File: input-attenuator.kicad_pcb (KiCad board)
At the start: 2 copper layers, 100.1 x 56.4 mm, 44 parts, among them J1 DC_INTF, J2 RF_IN, J3 RX_1_RF, J4 RX_2_RF, K1 EE2-5TNU-L, K2 EE2-5TNU-L, K3 EE2-5TNU-L, K4 EE2-5TNU-L, Q1 MMBT3904, Q2 MMBT3904, Q3 MMBT3904, Q4 MMBT3904, Q5 MMBT3904, Q6 MMBT3904, Q7 MMBT3904, Q8 MMBT3904, U1 74HC595

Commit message: relaysPlaced
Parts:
- added C3: 0.22u, Capacitor_SMD:C_0805_2012Metric, F.Cu at (132.0, 56.6)
- added C4: 0.22u, Capacitor_SMD:C_0805_2012Metric, F.Cu at (120.3, 56.6)
- added C5: 0.22u, Capacitor_SMD:C_0805_2012Metric, F.Cu at (98.5, 56.4)
- added C6: 0.22u, Capacitor_SMD:C_0805_2012Metric, F.Cu at (87.3, 56.4)
- added Q9: BC858, Package_TO_SOT_SMD:SOT-23, F.Cu at (87.8, 52.1)
- added R18: _, Resistor_SMD:R_0805_2012Metric, F.Cu at (87.3, 31.8)
- added R19: 14.0_, Resistor_SMD:R_0805_2012Metric, F.Cu at (84.7, 31.8)
- added R20: 14.0_, Resistor_SMD:R_0805_2012Metric, F.Cu at (82.2, 31.8)
- added R21: _, Resistor_SMD:R_0805_2012Metric, F.Cu at (79.7, 31.8)
- added R22: 22K, Resistor_SMD:R_0805_2012Metric, F.Cu at (122.6, 52.1)
- added R23: 22K, Resistor_SMD:R_0805_2012Metric, F.Cu at (128.7, 52.1)
- added R24: 22K, Resistor_SMD:R_0805_2012Metric, F.Cu at (93.6, 52.1)
- added R25: 22K, Resistor_SMD:R_0805_2012Metric, F.Cu at (99.7, 52.1)
- added R26: 22K, Resistor_SMD:R_0805_2012Metric, F.Cu at (78.7, 52.1)
- added R27: 22K, Resistor_SMD:R_0805_2012Metric, F.Cu at (84.7, 52.1)
- added R28: 1M, Resistor_SMD:R_0805_2012Metric, F.Cu at (132.0, 60.7)
- added R29: 1M, Resistor_SMD:R_0805_2012Metric, F.Cu at (98.5, 60.5)
- added R30: 1M, Resistor_SMD:R_0805_2012Metric, F.Cu at (87.3, 60.2)
- added U2: 74HC00, Package_SO:SO-14_3.9x8.65mm_P1.27mm, F.Cu at (92.9, 58.9)
- added U3: 74HC00, Package_SO:SO-14_3.9x8.65mm_P1.27mm, F.Cu at (82.0, 58.9)
- added U4: 74HC00, Package_SO:SO-14_3.9x8.65mm_P1.27mm, F.Cu at (126.4, 59.2)
- added U5: 74HC00, Package_SO:SO-14_3.9x8.65mm_P1.27mm, F.Cu at (105.1, 59.2)
- added U6: 74HC595, Package_SO:SO-16_5.3x10.2mm_P1.27mm, F.Cu at (70.6, 58.4)
- Q1, Q2, Q4, Q5, Q6, Q7, Q8: value MMBT3904 -> BC858
- R10, R6: value 22K -> 82.2
- R11, R15, R16, R5: value 22K -> _
- R12: value 40.9 -> 82.2
- R13: value 40.9 -> _
- R14: value 10.1 -> 14.0_
- R17: value 22K -> 14.0_
- R2: value 14.0 -> 22K
- R3: value 14.0 -> 1M
- R4: value 82.2 -> 14.0_
- R7: value 26.0 -> _
- R8: value 26.0 -> 14.0_
- R9: value 35.1 -> _
- U1: value 74HC595 -> 74HC00; footprint Package_SO:SO-16_5.3x10.2mm_P1.27mm -> Package_SO:SO-14_3.9x8.65mm_P1.27mm
- moved D8 88.0 mm to (77.1, 31.8), turned to 90 degrees
- moved J3 80.8 mm to (70.8, 40.6), turned to 90 degrees
- moved D7 79.4 mm to (76.1, 47.0), turned to 90 degrees
- moved J2 74.8 mm to (139.9, 49.3), turned to 135 degrees
- moved Q8 72.7 mm to (81.7, 52.1), turned to 90 degrees
- moved R17 72.0 mm to (94.7, 31.8), turned to -90 degrees
- moved R16 69.5 mm to (97.2, 31.8), turned to 90 degrees
- moved K4 62.4 mm to (83.2, 41.9), turned to 180 degrees
- moved R12 61.2 mm to (80.9, 28.4)
- moved R13 57.9 mm to (86.0, 28.4)
- moved J1 53.8 mm to (72.1, 75.4)
- moved R5 51.6 mm to (114.5, 31.8)
- moved Q7 49.1 mm to (102.8, 52.1), turned to 90 degrees
- moved Q3 48.1 mm to (120.8, 83.0)
- moved D6 46.7 mm to (92.1, 31.8), turned to 90 degrees
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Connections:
- C1 pad 1: VRelay -> +5V
- C2 pad 2: VRelay -> +5V
- D1 pad 1: VRelay -> Net-(D1-Pad1)
- D1 pad 2: Net-(D1-Pad2) -> GND
- D2 pad 1: VRelay -> Net-(D2-Pad1)
- D2 pad 2: Net-(D2-Pad2) -> GND
- D3 pad 1: VRelay -> Net-(D3-Pad1)
- D3 pad 2: Net-(D3-Pad2) -> GND
- D4 pad 1: VRelay -> Net-(D4-Pad1)
- D4 pad 2: Net-(D4-Pad2) -> GND
- D5 pad 1: VRelay -> Net-(D5-Pad1)
- D5 pad 2: Net-(D5-Pad2) -> GND
- D6 pad 1: VRelay -> Net-(D6-Pad1)
- D6 pad 2: Net-(D6-Pad2) -> GND
- D7 pad 1: VRelay -> Net-(D7-Pad1)
- D7 pad 2: Net-(D7-Pad2) -> GND
- D8 pad 1: VRelay -> Net-(D8-Pad1)
- D8 pad 2: Net-(D8-Pad2) -> GND
- J1 pad 1: VRelay -> +5V
- J2 pad 1: RF_IN -> /RF_TX
- J3 pad 1: RX_1_RF -> /RF_RX
- J4 pad 1: RX_2_RF -> /Antenna
- K1 pad 1: VRelay -> GND
- K1 pad 12: Net-(D1-Pad2) -> Net-(D2-Pad1)
- K1 pad 4: RF_IN -> Net-(K1-Pad4)
- K1 pad 6: VRelay -> GND
- K1 pad 7: Net-(D2-Pad2) -> Net-(D1-Pad1)
- K2 pad 1: VRelay -> GND
- K2 pad 10: Net-(K2-Pad10) -> /RF_TX
- K2 pad 12: Net-(D3-Pad2) -> Net-(D3-Pad1)
- K2 pad 3: Net-(K2-Pad10) -> /RF_TX
- K2 pad 4: Net-(K1-Pad9) -> /Antenna
- K2 pad 5: Net-(K2-Pad5) -> Net-(K1-Pad4)
- K2 pad 6: VRelay -> GND
- K2 pad 7: Net-(D4-Pad2) -> Net-(D4-Pad1)
- K2 pad 8: Net-(K2-Pad8) -> Net-(K1-Pad4)
- K2 pad 9: Net-(K2-Pad9) -> /Antenna
- K3 pad 1: VRelay -> GND
- K3 pad 12: Net-(D5-Pad2) -> Net-(D5-Pad1)
- K3 pad 4: Net-(K2-Pad9) -> Net-(K1-Pad9)
- K3 pad 6: VRelay -> GND
- K3 pad 7: Net-(D6-Pad2) -> Net-(D6-Pad1)
- K4 pad 1: VRelay -> GND
- K4 pad 10: GND -> Net-(K4-Pad10)
- K4 pad 12: Net-(D7-Pad2) -> Net-(D7-Pad1)
- K4 pad 3: Net-(K3-Pad9) -> Net-(K4-Pad10)
- K4 pad 4: RX_1_RF -> Net-(K3-Pad9)
- K4 pad 5: GND -> Net-(K4-Pad5)
- K4 pad 6: VRelay -> GND
- K4 pad 7: Net-(D8-Pad2) -> Net-(D8-Pad1)
- K4 pad 8: Net-(K3-Pad9) -> Net-(K4-Pad8)
- K4 pad 9: RX_2_RF -> /RF_RX
- Q1 pad 2: GND -> +5V
- Q1 pad 3: Net-(D1-Pad2) -> Net-(D2-Pad1)
- Q2 pad 2: GND -> +5V
- Q2 pad 3: Net-(D2-Pad2) -> Net-(D1-Pad1)
- Q3 pad 1: Net-(Q3-Pad1) -> unconnected-(Q3-Pad1)
- Q3 pad 2: GND -> unconnected-(Q3-Pad2)
- Q3 pad 3: Net-(D3-Pad2) -> unconnected-(Q3-Pad3)
- Q4 pad 2: GND -> +5V
- Q4 pad 3: Net-(D4-Pad2) -> Net-(D3-Pad1)
- Q5 pad 2: GND -> +5V
- Q5 pad 3: Net-(D5-Pad2) -> Net-(D4-Pad1)
- Q6 pad 2: GND -> +5V
- Q6 pad 3: Net-(D6-Pad2) -> Net-(D5-Pad1)
- Q7 pad 2: GND -> +5V
- Q7 pad 3: Net-(D7-Pad2) -> Net-(D6-Pad1)
- Q8 pad 2: GND -> +5V
- Q8 pad 3: Net-(D8-Pad2) -> Net-(D7-Pad1)
- R1 pad 1: A1_ON -> Net-(R1-Pad1)
- R10 pad 1: A2_OFF -> Net-(R10-Pad1)
- R10 pad 2: Net-(Q4-Pad1) -> GND
- R11 pad 1: A3_ON -> Net-(R10-Pad1)
- R11 pad 2: Net-(Q5-Pad1) -> GND
- R12 pad 2: Net-(K3-Pad8) -> GND
- R13 pad 1: Net-(K3-Pad5) -> Net-(R12-Pad1)
- R13 pad 2: Net-(R12-Pad1) -> GND
- R14 pad 1: Net-(R12-Pad1) -> Net-(K3-Pad5)
- R14 pad 2: GND -> Net-(R10-Pad1)
- R15 pad 1: A3_OFF -> Net-(K3-Pad5)
- R15 pad 2: Net-(Q6-Pad1) -> Net-(R10-Pad1)
- R16 pad 1: RX_1_ON -> Net-(K3-Pad8)
- R16 pad 2: Net-(Q7-Pad1) -> Net-(R10-Pad1)
- R17 pad 1: RX_2_ON -> Net-(R10-Pad1)
- R17 pad 2: Net-(Q8-Pad1) -> Net-(K3-Pad8)
- R2 pad 2: Net-(K1-Pad8) -> Net-(Q2-Pad1)
- R3 pad 1: Net-(K1-Pad5) -> Net-(R3-Pad1)
- R3 pad 2: Net-(R2-Pad1) -> Net-(R3-Pad2)
- R4 pad 1: Net-(R2-Pad1) -> Net-(K1-Pad5)
- R4 pad 2: GND -> Net-(R4-Pad2)
- R5 pad 1: A1_OFF -> Net-(K1-Pad5)
- R5 pad 2: Net-(Q2-Pad1) -> Net-(R4-Pad2)
- R6 pad 1: A2_ON -> Net-(R4-Pad2)
- R6 pad 2: Net-(Q3-Pad1) -> GND
- R7 pad 1: Net-(R7-Pad1) -> Net-(R4-Pad2)
- R7 pad 2: Net-(K2-Pad8) -> GND
- R8 pad 1: Net-(K2-Pad5) -> Net-(R4-Pad2)
- R8 pad 2: Net-(R7-Pad1) -> Net-(K1-Pad8)
- R9 pad 1: Net-(R7-Pad1) -> Net-(K1-Pad8)
- R9 pad 2: GND -> Net-(R4-Pad2)
- U1 pad 1: A1_OFF -> Net-(R3-Pad1)
- U1 pad 10: VRelay -> Net-(U1-Pad10)
- U1 pad 11: Net-(J1-Pad4) -> Net-(U1-Pad10)
- U1 pad 12: Net-(J1-Pad5) -> Net-(R3-Pad2)
- U1 pad 13: GND -> Net-(R3-Pad2)
- U1 pad 14: Net-(J1-Pad3) -> +5V
- U1 pad 2: A2_ON -> Net-(R3-Pad1)
- U1 pad 3: A2_OFF -> Net-(U1-Pad3)
- U1 pad 4: A3_ON -> Net-(U1-Pad3)
- U1 pad 5: A3_OFF -> Net-(R3-Pad2)
- U1 pad 6: RX_1_ON -> Net-(R2-Pad1)
- U1 pad 7: RX_2_ON -> GND
- U1 pad 8: GND -> Net-(R1-Pad1)
- U1 pad 9: Net-(J1-Pad6) -> Net-(R3-Pad1)
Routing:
- net Net-(U4-Pad1): track 0.00 -> 43.4 mm
- net Net-(R30-Pad1): track 0.00 -> 38.2 mm
- net VRelay: track 26.6 -> 0.00 mm
- net /Antenna: track 0.00 -> 21.8 mm
- net Net-(R3-Pad2): track 0.00 -> 20.6 mm
- net Net-(C3-Pad1): track 0.00 -> 20.6 mm
- net Net-(R3-Pad1): track 0.00 -> 19.9 mm
- net /RF_TX: track 0.00 -> 19.1 mm
- net Net-(C5-Pad1): track 0.00 -> 19.0 mm
- net Net-(R29-Pad1): track 0.00 -> 18.4 mm
- net Net-(K1-Pad4): track 0.00 -> 15.3 mm
- net Net-(C6-Pad1): track 0.00 -> 14.1 mm
- net powerDown: track 0.00 -> 13.1 mm
- net Net-(K2-Pad5): track 12.6 -> 0.00 mm
- net Net-(R10-Pad1): track 0.00 -> 11.9 mm
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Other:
- board size 100.1 x 56.4 mm -> 102.4 x 86.1 mm

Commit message: lookAtC
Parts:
- added C7: 0.22u, Capacitor_SMD:C_0805_2012Metric, F.Cu at (147.2, 70.4)
- added C8: 2200u, Capacitor_THT:CP_Radial_D12.5mm_P7.50mm, F.Cu at (96.8, 72.4)
- added D10: S1BB, Diode_SMD:D_SMB_Handsoldering, F.Cu at (140.2, 61.4)
- added D9: 1N4148WS, Diode_SMD:D_SOD-323, F.Cu at (160.4, 63.1)
- added J2: DC_INTF, Connector_PinHeader_2.54mm:PinHeader_1x07_P2.54mm_Vertical, F.Cu at (67.8, 75.9)
- added Q10: MMBT3904, Package_TO_SOT_SMD:SOT-23, F.Cu at (137.2, 74.7)
- added R31: 3M3, Resistor_SMD:R_0805_2012Metric, F.Cu at (156.0, 63.1)
- added R32: 470k, Resistor_SMD:R_0805_2012Metric, F.Cu at (147.2, 73.3)
- added R33: 1M, Resistor_SMD:R_0805_2012Metric, F.Cu at (146.0, 76.3)
- added R34: 1M, Resistor_SMD:R_0805_2012Metric, F.Cu at (141.6, 73.9)
- added R35: 1M, Resistor_SMD:R_0805_2012Metric, F.Cu at (131.6, 76.2)
- added R36: 1M, Resistor_SMD:R_0805_2012Metric, F.Cu at (127.2, 76.2)
- added R37: 1M, Resistor_SMD:R_0805_2012Metric, F.Cu at (151.6, 73.3)
- added R38: 1M, Resistor_SMD:R_0805_2012Metric, F.Cu at (156.0, 66.0)
- added R39: 1M, Resistor_SMD:R_0805_2012Metric, F.Cu at (151.6, 70.3)
- added R40: 220k, Resistor_SMD:R_0805_2012Metric, F.Cu at (160.5, 60.1)
- added R41: 100k, Resistor_SMD:R_0805_2012Metric, F.Cu at (156.0, 60.1)
- added U7: TPS7A4501DCQT, Package_TO_SOT_SMD:SOT-223-6, F.Cu at (140.0, 68.3)
- added U8: LP339, Package_SO:SO-14_3.9x8.65mm_P1.27mm, F.Cu at (149.6, 63.8)
- C1: value 100u -> 2200u; footprint Capacitor_SMD:CP_Elec_6.3x5.4_Nichicon -> Capacitor_THT:CP_Radial_D12.5mm_P7.50mm
- J1: footprint Connector_PinHeader_2.54mm:PinHeader_1x06_P2.54mm_Vertical -> Connector_PinHeader_2.54mm:PinHeader_1x07_P2.54mm_Vertical
- moved C2 50.3 mm to (145.8, 81.0)
- moved Q3 38.4 mm to (157.5, 71.6)
- moved C1 32.6 mm to (112.0, 72.6)
- moved J1 8.39 mm to (67.3, 68.6), turned to 90 degrees
- renumbered J2 to J5
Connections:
- C1 pad 1: +5V -> /Vin2
- J1 pad 1: +5V -> /Vin
- Q3 pad 1: unconnected-(Q3-Pad1) -> Net-(Q3-Pad1)
- Q3 pad 2: unconnected-(Q3-Pad2) -> GND
- Q3 pad 3: unconnected-(Q3-Pad3) -> /PowerDn
- U5 pad 10: powerDown -> /PowerDn
- U5 pad 12: powerDown -> /PowerDn
- U5 pad 2: powerDown -> /PowerDn
- U5 pad 4: powerDown -> /PowerDn
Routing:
- net powerDown: track 13.1 -> 0.00 mm
- net /PowerDn: track 0.00 -> 13.1 mm

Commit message: lookAtCx
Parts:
- moved C2 60.7 mm to (101.6, 122.7)
- moved R31 60.7 mm to (111.8, 104.7)
- moved R38 60.7 mm to (111.8, 107.7)
- moved R40 60.7 mm to (116.2, 101.8)
- moved R41 60.7 mm to (111.8, 101.8)
- moved U7 60.7 mm to (95.8, 110.0)
- moved D9 60.7 mm to (116.2, 104.7)
- moved R32 60.7 mm to (103.0, 115.0)
- moved R37 60.7 mm to (107.4, 115.0)
- moved U8 60.7 mm to (105.4, 105.4)
- moved C7 60.7 mm to (103.0, 112.0)
- moved D10 60.7 mm to (96.0, 103.1)
- moved Q10 60.7 mm to (93.0, 116.4)
- moved Q3 60.7 mm to (113.3, 113.3)
- moved R33 60.7 mm to (101.8, 118.0)
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
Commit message: final
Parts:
- U6: footprint Package_SO:SO-16_5.3x10.2mm_P1.27mm -> Package_SO:SO-16_3.9x9.9mm_P1.27mm
- moved J2 73.4 mm to (129.8, 69.3)
- moved R33 61.0 mm to (133.9, 66.0), turned to 180 degrees
- moved R32 60.0 mm to (137.7, 66.0), turned to 180 degrees
- moved Q10 59.3 mm to (134.4, 73.9), turned to 90 degrees
- moved U8 57.9 mm to (143.3, 61.6)
- moved C2 57.3 mm to (91.4, 66.3), turned to 90 degrees
- moved R31 53.5 mm to (138.2, 58.2), turned to 90 degrees
- moved J1 52.8 mm to (110.0, 69.3)
- moved R34 50.0 mm to (89.2, 66.3), turned to -90 degrees
- moved R39 48.8 mm to (137.9, 73.9), turned to 90 degrees
- moved Q3 48.3 mm to (141.2, 73.9)
- moved R37 47.6 mm to (91.4, 70.1), turned to -90 degrees
- moved R38 45.2 mm to (93.7, 66.3), turned to 90 degrees
- moved C7 44.1 mm to (89.2, 70.1), turned to 90 degrees
- moved U7 43.0 mm to (82.5, 69.1), turned to 180 degrees
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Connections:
- R31 pad 1: Net-(R31-Pad1) -> /PowerDn
- R33 pad 1: Net-(R31-Pad1) -> /PowerDn
- U6 pad 1: 5dB -> 20dB
- U6 pad 11: Net-(J1-Pad4) -> Net-(J1-Pad5)
- U6 pad 12: Net-(J1-Pad5) -> Net-(J1-Pad4)
- U6 pad 3: 20dB -> 5dB
- U8 pad 1: /PowerDn -> (no net)
- U8 pad 2: Net-(R31-Pad1) -> /PowerDn
- U8 pad 6: +5V -> (no net)
- U8 pad 7: Net-(R31-Pad1) -> (no net)
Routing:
- net +5V: track 0.00 -> 226.6 mm, vias 0 -> 8
- net GND: track 6.49 -> 171.0 mm, vias 0 -> 15
- net /Vin2: track 0.00 -> 139.3 mm
- net Net-(D1-Pad1): track 0.00 -> 102.0 mm
- net /PowerDn: track 13.1 -> 105.4 mm, vias 0 -> 2
- net Net-(D4-Pad1): track 0.00 -> 61.4 mm
- net /SHDN: track 0.00 -> 58.0 mm, vias 0 -> 1
- net Net-(Q7-Pad1): track 2.89 -> 49.0 mm
- net /Vin: track 0.00 -> 44.9 mm, vias 0 -> 3
- net Net-(J1-Pad6): track 0.00 -> 39.9 mm
- net Net-(J1-Pad4): track 0.00 -> 37.4 mm
- net Net-(J1-Pad3): track 0.00 -> 34.9 mm
- net Net-(Q9-Pad1): track 2.89 -> 28.3 mm
- net Net-(D6-Pad1): track 0.00 -> 25.3 mm
- net Net-(R31-Pad2): track 0.00 -> 19.9 mm
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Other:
- board size 102.4 x 86.1 mm -> 102.6 x 109.5 mm

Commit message: moved
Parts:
- moved Q9 5.34 mm to (71.3, 34.0)
- moved Q7 5.34 mm to (76.6, 34.0)
- moved D5 2.81 mm to (93.2, 48.3)
- moved J3 2.59 mm to (73.9, 40.4)
- moved J5 2.58 mm to (142.2, 48.3)
- moved D2 2.44 mm to (108.5, 46.7)
- moved D6 2.44 mm to (93.9, 32.0)
- moved D1 2.44 mm to (109.3, 31.5)
- moved D8 2.44 mm to (79.6, 31.5)
- moved R10 2.44 mm to (103.2, 28.4)
- moved R11 2.44 mm to (98.7, 28.4)
- moved R12 2.44 mm to (83.4, 28.2)
- moved R13 2.44 mm to (88.4, 28.2)
- moved R14 2.44 mm to (102.2, 31.5)
- moved R15 2.44 mm to (104.7, 31.5)
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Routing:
- net Net-(Q7-Pad1): track 49.0 -> 43.7 mm
- net Net-(Q9-Pad1): track 28.3 -> 23.7 mm
- net Net-(D6-Pad1): track 25.3 -> 29.7 mm
- net +5V: track 226.6 -> 222.4 mm
- net GND: track 171.0 -> 173.1 mm
- net Net-(R27-Pad1): track 12.9 -> 11.1 mm
- net Net-(D8-Pad1): track 12.7 -> 14.1 mm
- net Net-(D1-Pad1): track 102.0 -> 103.2 mm
- net Net-(D4-Pad1): track 61.4 -> 62.6 mm
- net Net-(D5-Pad1): track 8.42 -> 7.55 mm
- net Net-(D3-Pad1): track 7.24 -> 8.04 mm

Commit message: vias
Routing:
- net GND: track 173.1 -> 162.7 mm, vias 15 -> 17
- net /SHDN: track 58.0 -> 61.2 mm, vias 1 -> 3
- net Net-(J1-Pad4): track 37.4 -> 40.0 mm, vias 0 -> 1
- net Net-(J1-Pad3): track 34.9 -> 37.5 mm, vias 0 -> 1
- net Net-(J1-Pad5): track 17.2 -> 19.2 mm, vias 0 -> 1
- net Net-(J1-Pad6): track 39.9 -> 41.9 mm, vias 0 -> 1
- net /Vin: track 44.9 -> 47.0 mm, vias 3 -> 4
- net /RF_RX: track 8.09 -> 9.61 mm, vias 0 -> 3
- net /Antenna: track 21.8 -> 23.3 mm, vias 0 -> 3
- net /RF_TX: track 18.7 -> 20.1 mm, vias 0 -> 3

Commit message: Added edge cuts, mounting holes and improved silkscreen
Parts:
- added H1: MountingHole_Pad, MountingHole:MountingHole_3.2mm_M3_ISO7380_Pad, F.Cu at (149.6, 78.5)
- added H2: MountingHole_Pad, MountingHole:MountingHole_3.2mm_M3_ISO7380_Pad, F.Cu at (149.6, 29.0)
- added H3: MountingHole_Pad, MountingHole:MountingHole_3.2mm_M3_ISO7380_Pad, F.Cu at (67.6, 78.5)
- added H4: MountingHole_Pad, MountingHole:MountingHole_3.2mm_M3_ISO7380_Pad, F.Cu at (67.6, 29.0)
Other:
- board size 102.6 x 109.5 mm -> 90.2 x 57.7 mm

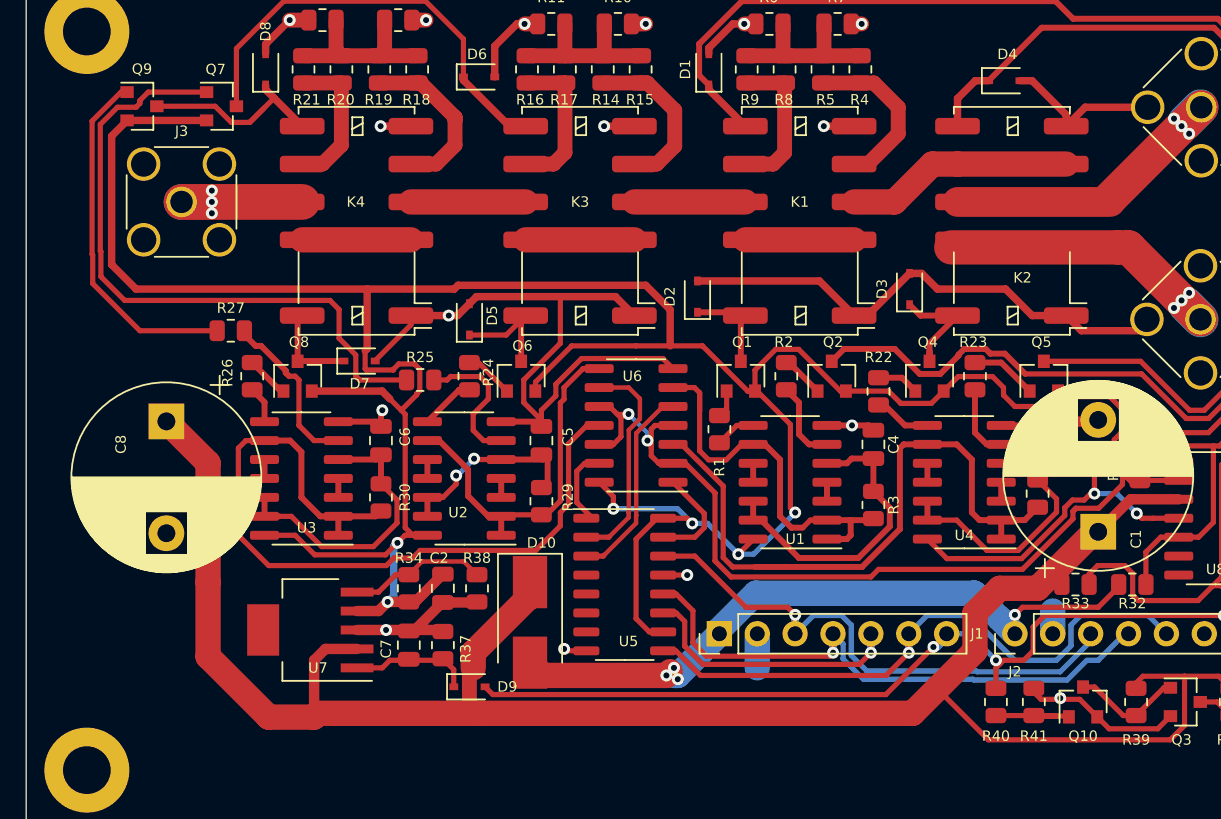
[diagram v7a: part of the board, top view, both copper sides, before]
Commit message: DRC: moved some errors as warning (silkscreen and courtyard) and made small tracks adjustment
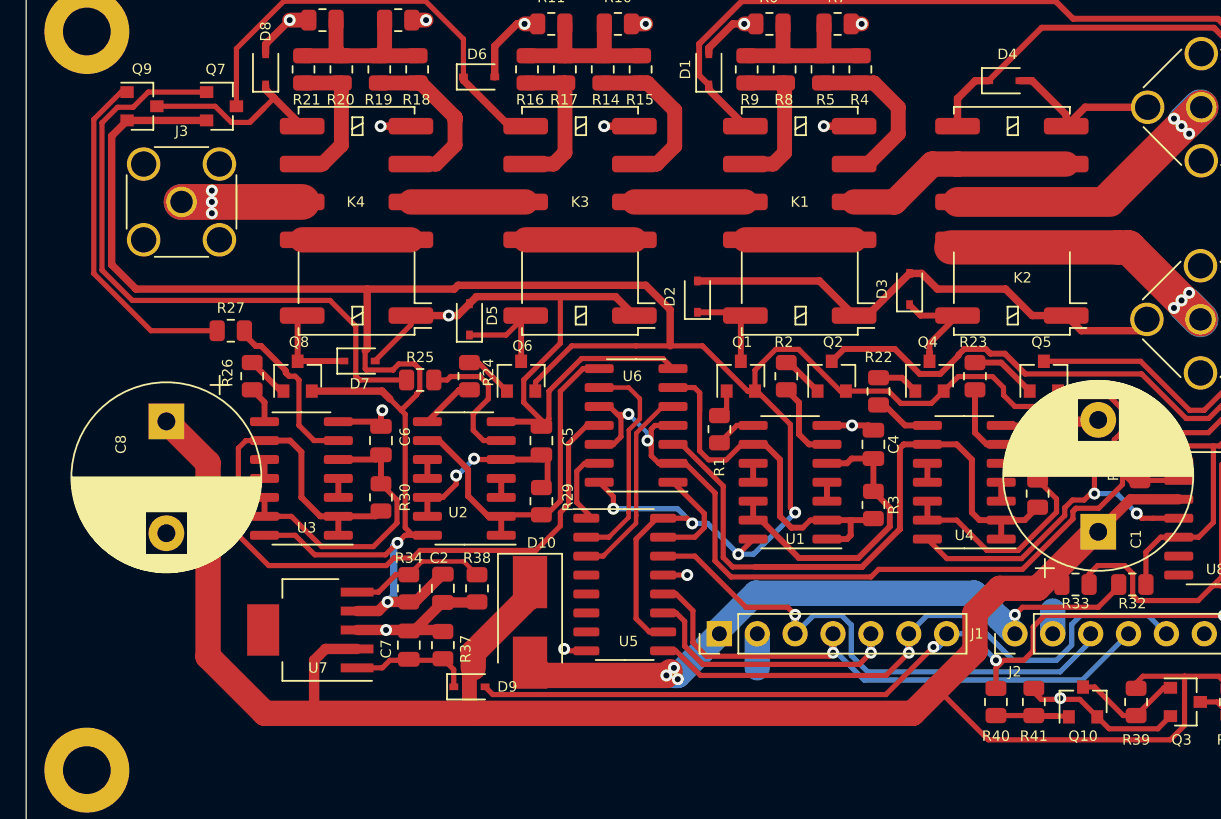
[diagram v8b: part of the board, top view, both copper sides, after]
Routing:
- net Net-(Q9-Pad1): track 23.7 -> 23.2 mm
- net Net-(Q7-Pad1): track 43.7 -> 43.2 mm
